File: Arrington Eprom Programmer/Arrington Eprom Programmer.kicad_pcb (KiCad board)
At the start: 2 copper layers, 71.4 x 53.3 mm, 19 parts, among them J1 PGM volt in, J2 DB25_Male, SW1 SW_SPDT, U1 74LS164, U2 2716, U3 74LS299, U4 4N35

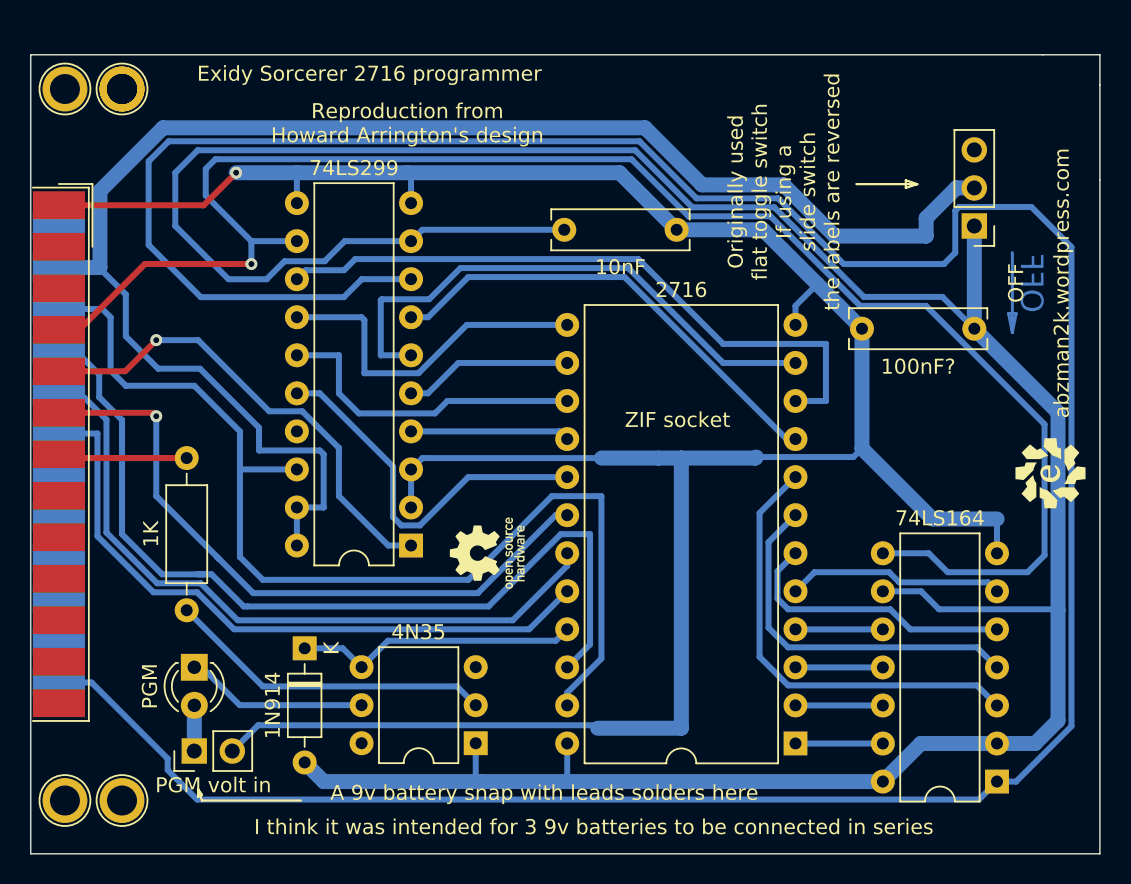
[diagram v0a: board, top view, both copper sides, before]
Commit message: updates to be closer to real one
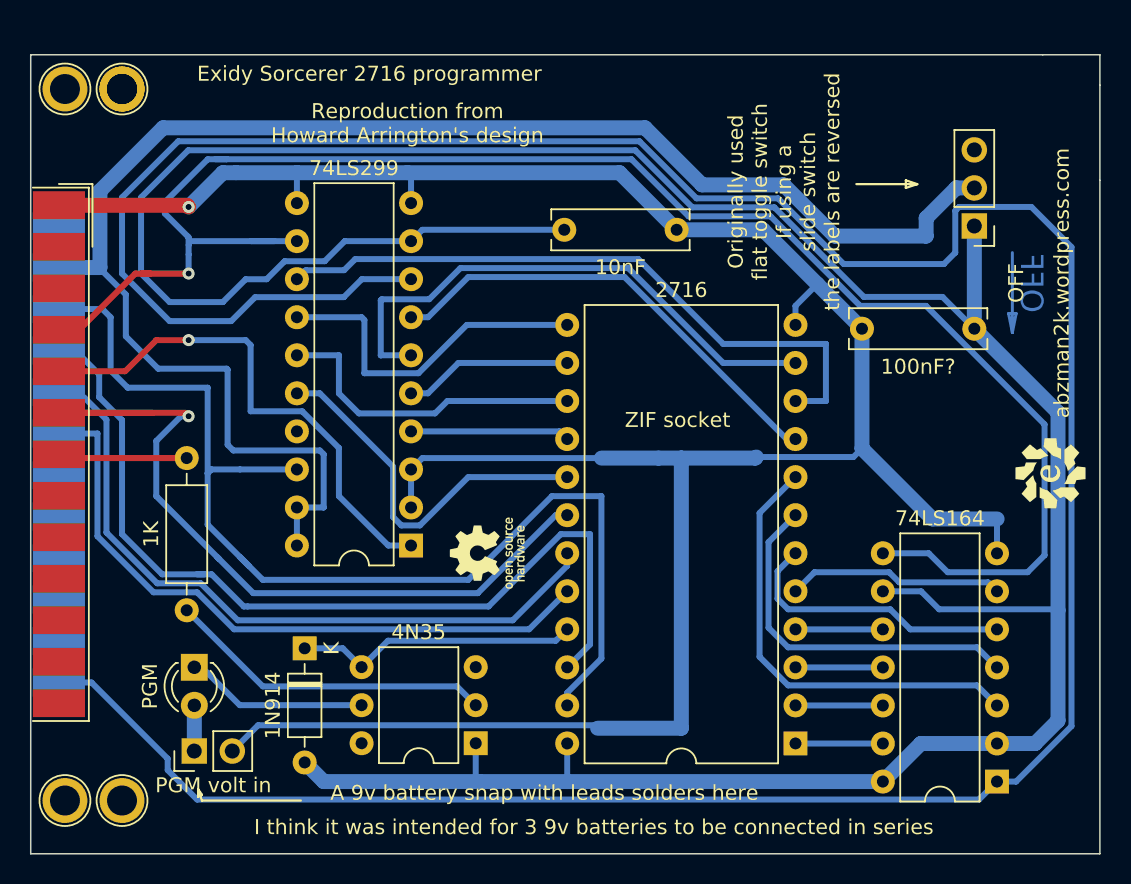
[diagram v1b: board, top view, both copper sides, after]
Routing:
- net /Out5: track 44.4 -> 54.0 mm
- net /switched power: track 196.5 -> 203.3 mm
- net /In7: track 200.2 -> 204.8 mm
- net /Out7: track 109.4 -> 113.3 mm
- net /Out0: track 71.7 -> 75.3 mm
- net /Out6: track 31.9 -> 34.5 mm
- net VCC: track 106.2 -> 108.3 mm
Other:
- board text added: "Out0: SL / A8 Out1: A9 Out2: A10 Out3: ~OE Out4: ~PGM Out5: ~CE Out6: S0 Out7: Clock In7: From299 In7: To164"
- board text removed: "Out0: SL / A8 Out1: A9 Out2: A10 Out3: ~OE Out4: PGM Out5: ~CE Out6: S0 Out7: Clock In7: From299 In7: To164"

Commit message: updated some DRC stuff
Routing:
- net /Out5: track 54.0 -> 47.6 mm
- net /Out7: track 113.3 -> 111.0 mm
- net /Out0: track 75.3 -> 74.4 mm
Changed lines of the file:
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@@
   (via (at 95.885 86.995) (size 0.8) (drill 0.4) (layers "F.Cu" "B.Cu") (net 8))
   (segment (start 95.8265 84.5135) (end 94.2975 82.9845) (width 0.4) (layer "B.Cu") (net 8))
-  (segment (start 100.081 84.831) (end 101.6 84.831) (width 0.4) (layer "B.Cu") (net 8))
   (segment (start 151.892 106.934) (end 146.558 106.934) (width 0.4) (layer "B.Cu") (net 8))
   (segment (start 146.558 106.934) (end 145.293 105.669) (width 0.4) (layer "B.Cu") (net 8))
@@
   (segment (start 98.425 79.36448) (end 97.16552 79.36448) (width 0.4) (layer "B.Cu") (net 8))
   (segment (start 95.885 84.572) (end 95.8265 84.5135) (width 0.4) (layer "B.Cu") (net 8))
-  (segment (start 97.67352 79.36448) (end 98.425 79.36448) (width 0.4) (layer "B.Cu") (net 8))
   (segment (start 145.115634 89.154) (end 153.02448 97.062846) (width 0.4) (layer "B.Cu") (net 8))
   (segment (start 145.293 105.669) (end 142.23 105.669) (width 0.4) (layer "B.Cu") (net 8))
-  (segment (start 100.076 84.836) (end 100.081 84.831) (width 0.4) (layer "B.Cu") (net 8))
   (segment (start 129.260846 83.17448) (end 134.73648 83.17448) (width 0.4) (layer "B.Cu") (net 8))
   (segment (start 98.425 79.36448) (end 125.450846 79.36448) (width 0.4) (layer "B.Cu") (net 8))
@@
   (segment (start 99.695 91.44) (end 95.885 91.44) (width 0.4) (layer "B.Cu") (net 9))
   (segment (start 87.2265 96.29) (end 95.655 96.29) (width 0.4) (layer "F.Cu") (net 10))
-  (segment (start 87.2265 96.29) (end 93.496 96.29) (width 0.4) (layer "F.Cu") (net 10))
   (segment (start 95.655 96.29) (end 95.885 96.52) (width 0.4) (layer "F.Cu") (net 10))
   (via (at 95.885 96.52) (size 0.8) (drill 0.4) (layers "F.Cu" "B.Cu") (net 10))
-  (segment (start 97.917 106.045) (end 97.79 105.918) (width 0.4) (layer "B.Cu") (net 10))
   (segment (start 93.726 101.854) (end 93.726 98.171) (width 0.4) (layer "B.Cu") (net 10))
   (segment (start 97.917 106.045) (end 93.726 101.854) (width 0.4) (layer "B.Cu") (net 10))
@@
   (segment (start 123.444 101.854) (end 120.142 101.854) (width 0.4) (layer "B.Cu") (net 20))
   (segment (start 90.678 89.916) (end 90.127 89.365) (width 0.4) (layer "B.Cu") (net 20))
-  (segment (start 99.8855 106.4895) (end 99.314 105.918) (width 0.4) (layer "B.Cu") (net 20))
   (segment (start 114.554 107.442) (end 100.838 107.442) (width 0.4) (layer "B.Cu") (net 20))
-  (segment (start 99.319 100.071) (end 99.314 100.076) (width 0.4) (layer "B.Cu") (net 20))
   (segment (start 91.821 94.615) (end 90.678 93.472) (width 0.4) (layer "B.Cu") (net 20))
   (segment (start 97.155 94.615) (end 91.821 94.615) (width 0.4) (layer "B.Cu") (net 20))
